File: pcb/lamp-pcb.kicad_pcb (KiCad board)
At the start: 2 copper layers, 0 parts

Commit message: board geometry mostly figured out
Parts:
- added C1: 0.1uF, passive-smd:0603(1608m), F.Cu at (99.7, 127.6)
- added C10: 0.1uF, passive-smd:0603(1608m), F.Cu at (165.7, 95.2)
- added C11: 0.1uF, passive-smd:0603(1608m), F.Cu at (163.2, 98.4)
- added C2: 24pF, passive-smd:0603(1608m), F.Cu at (101.6, 130.2)
- added C3: 24pF, passive-smd:0603(1608m), F.Cu at (106.7, 130.2)
- added C4: 0.1uF, passive-smd:0603(1608m), F.Cu at (98.4, 126.4)
- added C5: 0.1uF, passive-smd:0603(1608m), F.Cu at (111.8, 119.4)
- added C6: 0.1uF, passive-smd:0603(1608m), F.Cu at (110.5, 118.1)
- added C7: 10uF, passive-smd:1206(3216m), F.Cu at (100.3, 173.4)
- added C8: 22uF, passive-smd:1206(3216m), F.Cu at (100.3, 163.2)
- added C9: 0.1uF, passive-smd:0603(1608m), F.Cu at (99.7, 116.2)
- added IC1: ATMEGA328P, qfp:TQFP32_P0.8mm, F.Cu at (115.6, 156.8)
- added IC2: LM1117, sot:SOT223, F.Cu at (100.3, 168.3)
- added IC3: TLC5973, soic:SOIC8, F.Cu at (182.9, 81.9)
- added J1: 5V_OUT, sip:SIP2, F.Cu at (138.4, 174.0)
- added J2: LED_CARD_BOTTOM, sip:SIP5, F.Cu at (158.1, 88.9)
- added LED1: CREE-CLV6A-FKB, led:PLCC6-SM-RGB-LED, F.Cu at (176.5, 102.9)
- added LED2: CREE-CLV6A-FKB, led:PLCC6-SM-RGB-LED, F.Cu at (177.8, 93.3)
- added LED3: HEART, led:0603(1608m)-SM-LED, F.Cu at (111.8, 127.6)
- added LED4: PWR, led:0603(1608m)-SM-LED, F.Cu at (143.5, 137.2)
- added P1: 7-12V_IN, sip:SIP2, F.Cu at (92.7, 174.0)
- added P2: AVR_ISP, connect-thru:2x3-ARRAY_P100mil, F.Cu at (129.5, 167.6)
- added P3: SERIAL, sip:SIP6, F.Cu at (115.6, 140.3)
- added P4: LEDSTACK, sip:SIP5, F.Cu at (115.6, 173.4)
- added P5: LEDSTACK, sip:SIP5, F.Cu at (104.1, 151.8)
- added P6: LEDSTACK, sip:SIP5, F.Cu at (127.0, 152.4)
- added P7: LED_CARD_TOP, sip:SIP5, F.Cu at (167.6, 81.9)
- added R1: 10kΩ, passive-smd:0603(1608m), F.Cu at (101.6, 114.3)
- added R2: 10kΩ, passive-smd:0603(1608m), F.Cu at (106.7, 114.3)
- added R3: 10kΩ, passive-smd:0603(1608m), F.Cu at (108.6, 116.2)
- added R4: 2kΩ, passive-smd:0603(1608m), F.Cu at (191.1, 86.4)
- added R5: 1kΩ, passive-smd:0603(1608m), F.Cu at (195.6, 85.1)
- added R6: 1kΩ, passive-smd:0603(1608m), F.Cu at (111.8, 125.7)
- added R7: 1kΩ, passive-smd:0603(1608m), F.Cu at (143.5, 141.0)
- added S1: TOP, switch:CK-JS102011SAQN_sm-spdt-switch, F.Cu at (196.2, 97.8)
- added Y1: 14.7456MHz, crystal:HC49_sm, F.Cu at (115.6, 167.6)

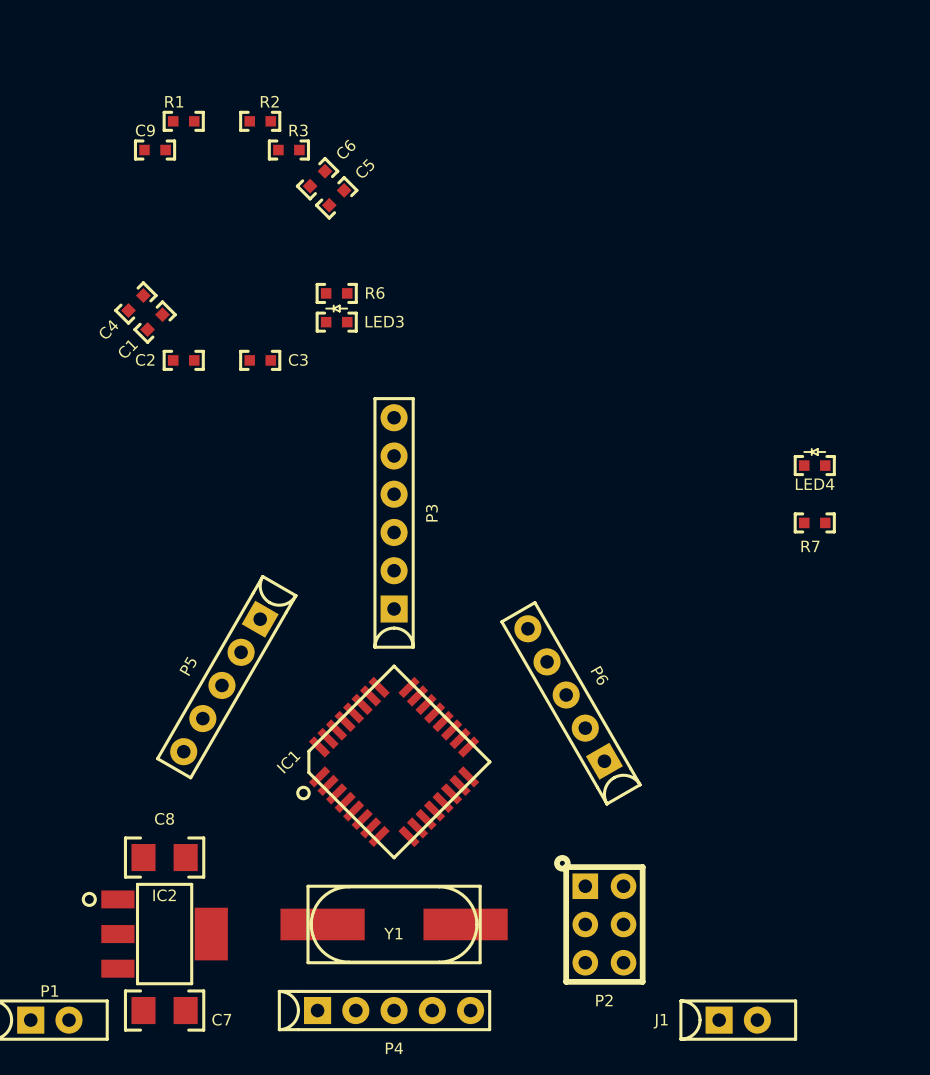
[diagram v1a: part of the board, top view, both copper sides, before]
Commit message: component positions good. need some mounting holes
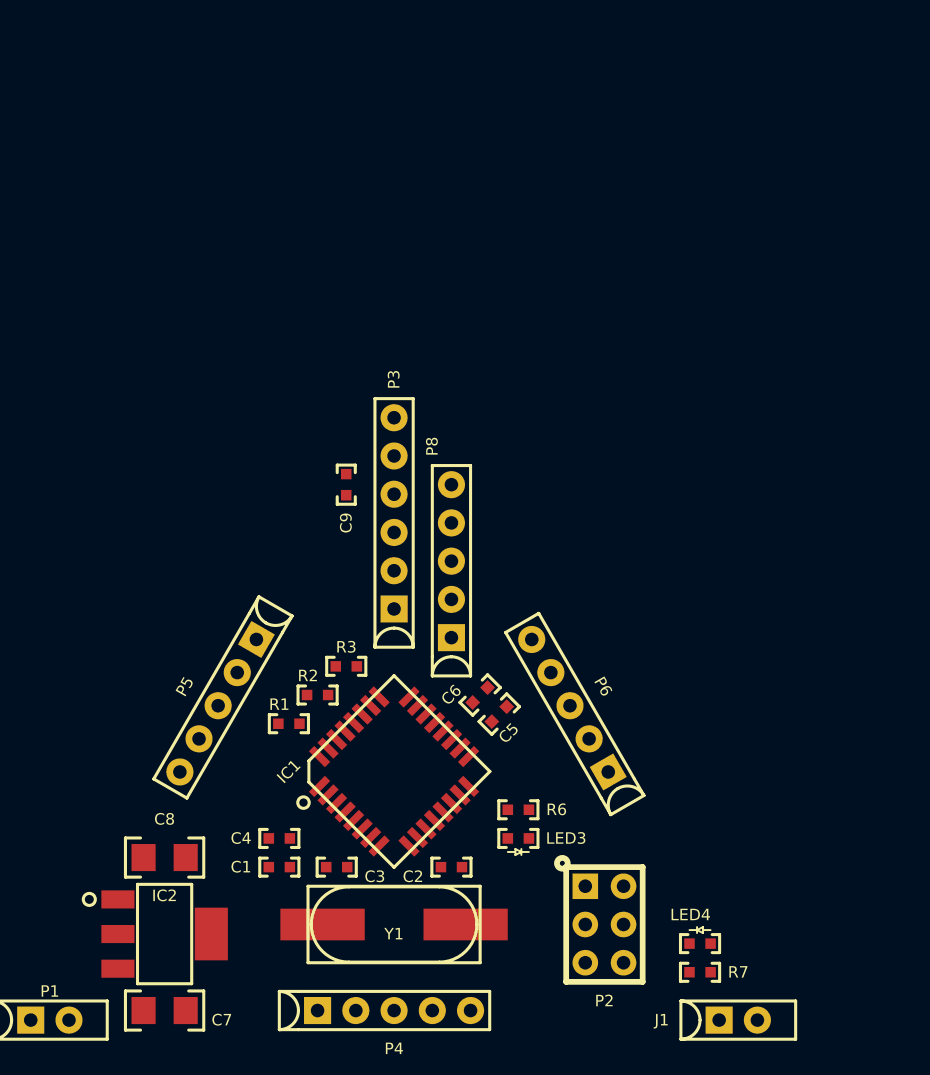
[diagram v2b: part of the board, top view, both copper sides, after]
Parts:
- added P8: SER_SHORT, sip:SIP5, F.Cu at (119.4, 143.5)
- moved R1 40.6 mm to (108.6, 154.3)
- moved R2 38.3 mm to (110.5, 152.4), turned to 180 degrees
- moved C2 38.1 mm to (119.4, 163.8), turned to 180 degrees
- moved C1 37.1 mm to (108.0, 163.8), turned to 180 degrees
- moved C4 36.8 mm to (108.0, 161.9), turned to 180 degrees
- moved LED3 36.4 mm to (123.8, 161.9), turned to 180 degrees
- moved R6 36.4 mm to (123.8, 160.0)
- moved C6 35.9 mm to (121.3, 152.4)
- moved C5 35.9 mm to (122.6, 153.7)
- moved R3 34.5 mm to (112.4, 150.5), turned to 180 degrees
- moved C3 34.0 mm to (111.8, 163.8), turned to 0 degrees
- moved LED4 32.7 mm to (135.9, 168.9)
- moved R7 30.8 mm to (135.9, 170.8)
- moved C9 25.6 mm to (112.4, 138.4), turned to 90 degrees
- moved P5 1.37 mm to (103.9, 153.1)
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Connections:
- IC1 pad 23: /STACKSENSE0 -> Net-(IC1-Pad23)
- IC1 pad 24: /STACKSENSE1 -> Net-(IC1-Pad24)
- IC1 pad 25: /STACKSENSE2 -> /STACKSENSE0
- IC1 pad 26: Net-(IC1-Pad26) -> /STACKSENSE1
- IC1 pad 27: Net-(IC1-Pad27) -> /STACKSENSE2

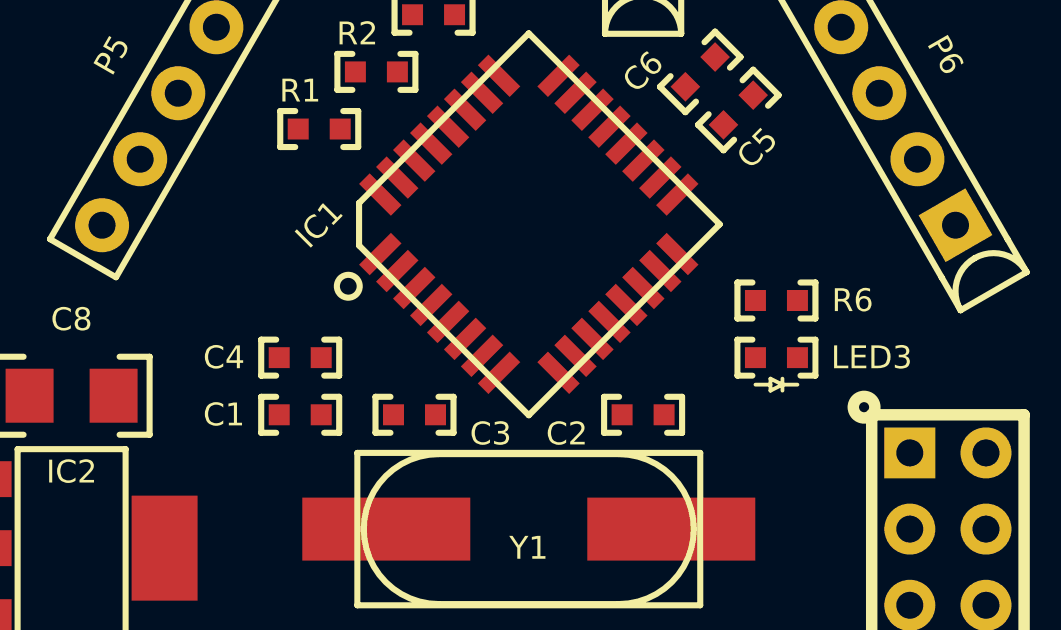
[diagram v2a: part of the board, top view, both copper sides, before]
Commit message: mounting holes
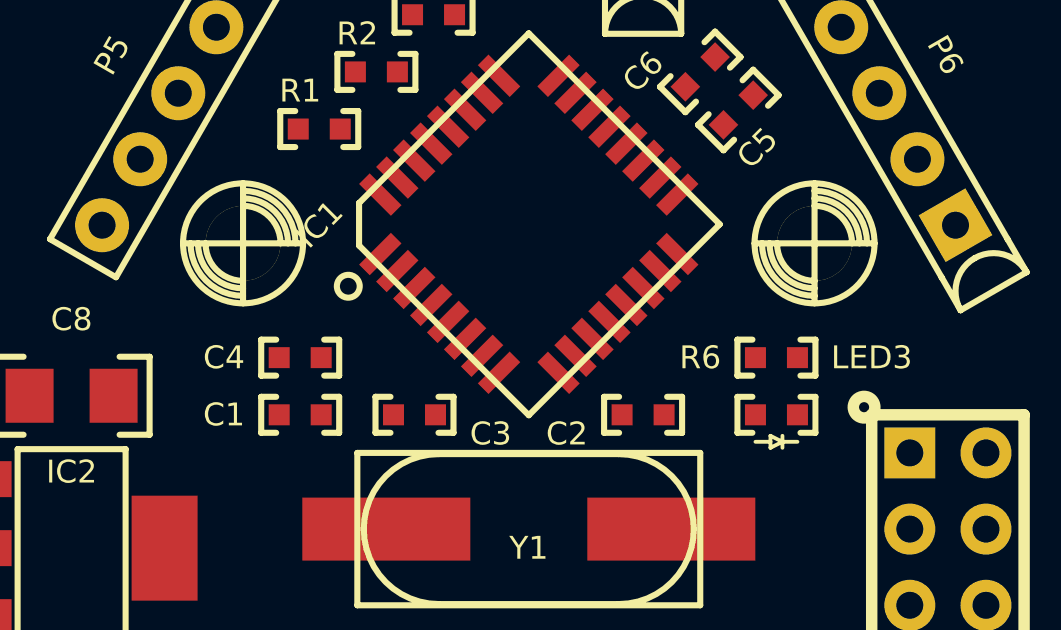
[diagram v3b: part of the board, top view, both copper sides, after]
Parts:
- added M2: Val**, asm:M2, F.Cu at (106.0, 158.1)
- added M2: Val**, asm:M2, F.Cu at (125.1, 158.1)
- moved LED3 1.91 mm to (123.8, 163.8)
- moved R6 1.91 mm to (123.8, 161.9)
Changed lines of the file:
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@@
 (kicad_pcb (version 3) (host pcbnew "(2014-02-03 BZR 4657)-product")
   (general
-    (links 100)
+    (links 0)
     (no_connects 100)
     (area 0 0 0 0)
@@
     (tracks 0)
     (zones 0)
-    (modules 37)
+    (modules 39)
     (nets 48)
   )
@@
   )
   (module "led:0603(1608m)-SM-LED" (layer F.Cu)
-    (at 123.825 161.925 180)
-    (solder_paste_margin -0.0254)
-    (attr smd)
-    (fp_text reference LED3 (at -3.175 0 180) (layer F.SilkS)
+    (at 123.825 163.83 180)
+    (solder_paste_margin -0.0254)
+    (attr smd)
+    (fp_text reference LED3 (at -3.175 1.905 180) (layer F.SilkS)
       (effects (font (size 0.762 0.762) (thickness 0.1524)))
     )
@@
   )
   (module "passive-smd:0603(1608m)" (layer F.Cu)
-    (at 123.825 160.02 180)
-    (solder_paste_margin -0.0254)
-    (attr smd)
-    (fp_text reference R6 (at -2.54 0 180) (layer F.SilkS)
+    (at 123.825 161.925 180)
+    (solder_paste_margin -0.0254)
+    (attr smd)
+    (fp_text reference R6 (at 2.54 0 180) (layer F.SilkS)
       (effects (font (size 0.762 0.762) (thickness 0.1524)))
     )
@@
       (net 20 /USART_TX))
   )
+  (module asm:M2 (layer F.Cu)
+    (at 106.045 158.115)
+    (fp_text reference M2 (at 0 0) (layer F.SilkS) hide
+      (effects (font (size 0.762 0.762) (thickness 0.1524)))
+    )
+    (fp_text value Val** (at 0 0) (layer F.SilkS) hide
+      (effects (font (size 0.762 0.762) (thickness 0.1524)))
+    )
+    (fp_arc (start 0 0) (end 0 1.25) (angle 90) (layer F.SilkS) (width 0.2032))
+    (fp_arc (start 0 0) (end 0 -1.25) (angle 90) (layer F.SilkS) (width 0.2032))
+    (fp_arc (start 0 0) (end 0 1.5) (angle 90) (layer F.SilkS) (width 0.2032))
+    (fp_arc (start 0 0) (end 0 1.75) (angle 90) (layer F.SilkS) (width 0.2032))
+    (fp_arc (start 0 0) (end 0 -1.5) (angle 90) (layer F.SilkS) (width 0.2032))
+    (fp_arc (start 0 0) (end 0 -1.75) (angle 90) (layer F.SilkS) (width 0.2032))
+    (fp_line (start 0 0) (end 0 2) (layer F.SilkS) (width 0.2032))
+    (fp_line (start 0 0) (end -2 0) (layer F.SilkS) (width 0.2032))
+    (fp_line (start 0 -2) (end 0 0) (layer F.SilkS) (width 0.2032))
+    (fp_line (start 0 0) (end 2 0) (layer F.SilkS) (width 0.2032))
+    (fp_circle (center 0 0) (end 2 0) (layer F.SilkS) (width 0.2032))
+    (pad "" thru_hole circle (at 0 0) (size 2.5 2.5) (drill 2.5) (layers *.Cu *.Mask F.SilkS))
+  )
+  (module asm:M2 (layer F.Cu)
+    (at 125.095 158.115)
+    (fp_text reference M2 (at 0 0) (layer F.SilkS) hide
+      (effects (font (size 0.762 0.762) (thickness 0.1524)))
+    )
+    (fp_text value Val** (at 0 0) (layer F.SilkS) hide
+      (effects (font (size 0.762 0.762) (thickness 0.1524)))
+    )
+    (fp_arc (start 0 0) (end 0 1.25) (angle 90) (layer F.SilkS) (width 0.2032))
+    (fp_arc (start 0 0) (end 0 -1.25) (angle 90) (layer F.SilkS) (width 0.2032))
+    (fp_arc (start 0 0) (end 0 1.5) (angle 90) (layer F.SilkS) (width 0.2032))
+    (fp_arc (start 0 0) (end 0 1.75) (angle 90) (layer F.SilkS) (width 0.2032))
+    (fp_arc (start 0 0) (end 0 -1.5) (angle 90) (layer F.SilkS) (width 0.2032))
+    (fp_arc (start 0 0) (end 0 -1.75) (angle 90) (layer F.SilkS) (width 0.2032))
+    (fp_line (start 0 0) (end 0 2) (layer F.SilkS) (width 0.2032))
+    (fp_line (start 0 0) (end -2 0) (layer F.SilkS) (width 0.2032))
+    (fp_line (start 0 -2) (end 0 0) (layer F.SilkS) (width 0.2032))
+    (fp_line (start 0 0) (end 2 0) (layer F.SilkS) (width 0.2032))
+    (fp_circle (center 0 0) (end 2 0) (layer F.SilkS) (width 0.2032))
+    (pad "" thru_hole circle (at 0 0) (size 2.5 2.5) (drill 2.5) (layers *.Cu *.Mask F.SilkS))
+  )
   (dimension 46.355 (width 0.254) (layer Eco2.User)

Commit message: laying traces
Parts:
- moved C4 75.2 mm to (92.7, 88.3)
- moved C1 74.6 mm to (92.7, 90.8)
- moved C2 74.6 mm to (104.1, 90.8)
- moved C3 74.6 mm to (96.5, 90.8)
- moved C6 74.6 mm to (106.0, 79.4)
- moved C9 74.6 mm to (97.2, 65.4)
- moved IC2 74.6 mm to (85.1, 95.2)
- moved J1 74.6 mm to (123.2, 101.0)
- moved LED3 74.6 mm to (108.6, 90.8)
- moved M2 74.6 mm to (90.8, 85.1)
- moved M2 74.6 mm to (109.9, 85.1)
- moved P1 74.6 mm to (77.5, 101.0)
- moved P3 74.6 mm to (100.3, 67.3)
- moved R1 74.6 mm to (93.3, 81.3)
- moved R2 74.6 mm to (95.2, 79.4)
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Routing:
- net VCC: track 0.00 -> 45.4 mm
- net /USART_TX: track 0.00 -> 32.8 mm, vias 0 -> 2
- net GND: track 0.00 -> 26.5 mm
- net /USART_RX: track 0.00 -> 25.7 mm, vias 0 -> 2
- net /AVR_RST: track 0.00 -> 20.0 mm, vias 0 -> 2
- net /AVR_SCK: track 0.00 -> 19.3 mm, vias 0 -> 1
- net /AVR_MOSI: track 0.00 -> 16.7 mm
- net /STACKSENSE1: track 0.00 -> 16.1 mm, vias 0 -> 1
- net /LEDSTACK1: track 0.00 -> 12.3 mm
- net /AVR_MISO: track 0.00 -> 11.6 mm
- net Net-(C9-Pad2): track 0.00 -> 11.5 mm
- net Net-(C2-Pad2): track 0.00 -> 10.9 mm
- net Net-(C3-Pad2): track 0.00 -> 7.10 mm
- net Net-(IC1-Pad13): track 0.00 -> 5.03 mm
- net /STACKSENSE2: track 0.00 -> 4.95 mm
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- added copper zone on F.Cu, net /VIN
- added copper zone on F.Cu, net VCC
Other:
- board outline added: 53.3 x 46.4 mm
- net class Default: via_dia 0.889 -> 0.762; via_drill 0.635 -> 0.381
- rule trace_min: 0.254 -> 0.1524
- rule via_min_drill: 0.508 -> 0.3556
- rule via_min_size: 0.889 -> 0.7112

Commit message: layout going well but computer dying
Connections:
- R4 pad 2: GND -> /LED_GND
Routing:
- net /STACKSENSE0: track 2.65 -> 41.5 mm, vias 0 -> 1
- net /LEDSTACK0: track 0.00 -> 32.6 mm, vias 0 -> 1
- net /LEDSTACK2: track 0.00 -> 19.6 mm, vias 0 -> 1
- net VCC: track 45.4 -> 64.8 mm
- net /STACKSENSE2: track 4.95 -> 21.6 mm, vias 0 -> 1
- added copper zone on B.Cu, net GND
- added copper zone on F.Cu, net GND
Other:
- outline, holes or cut-outs redrawn

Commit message: layout done. getting quotes then gonna clean up
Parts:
- added M2: Val**, asm:M2, F.Cu at (176.5, 144.8)
- added M2: Val**, asm:M2, F.Cu at (154.9, 127.0)
- moved R4 57.0 mm to (175.5, 141.2), turned to 270 degrees
- moved J2 57.0 mm to (165.7, 145.4)
- moved S1 56.2 mm to (154.9, 135.9), turned to 270 degrees
- moved IC3 54.5 mm to (175.3, 135.9), turned to 270 degrees
- moved LED2 47.9 mm to (165.7, 139.7), turned to 180 degrees
- moved C11 47.5 mm to (156.2, 145.4), turned to 180 degrees
- moved C10 47.4 mm to (177.2, 141.2), turned to 90 degrees
- moved R5 46.0 mm to (175.3, 126.4), turned to 180 degrees
- moved P7 44.5 mm to (165.7, 126.4)
- moved LED1 31.1 mm to (165.7, 132.1), turned to 180 degrees
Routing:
- net /VIN: track 0.00 -> 74.9 mm, vias 0 -> 1
- net VCC: track 64.8 -> 120.2 mm
- net /VLOG: track 0.00 -> 36.0 mm, vias 0 -> 2
- net /SENSE_TOP: track 0.00 -> 35.9 mm, vias 0 -> 1
- net /VLED: track 0.00 -> 30.6 mm
- net GND: track 26.5 -> 52.9 mm, vias 0 -> 3
- net /AVR_RST: track 20.0 -> 43.7 mm, vias 2 -> 3
- net /SENSE_BOT: track 0.00 -> 23.0 mm, vias 0 -> 1
- net /LED_SER_OUT: track 0.00 -> 22.0 mm, vias 0 -> 2
- net Net-(LED1-Pad5): track 0.00 -> 12.4 mm
- net Net-(LED1-Pad4): track 0.00 -> 12.0 mm
- net Net-(LED1-Pad6): track 0.00 -> 11.1 mm
- net /LED_SER_IN: track 0.00 -> 10.9 mm
- net /VLOG_TOP: track 0.00 -> 10.8 mm, vias 0 -> 1
- net /RED: track 0.00 -> 10.6 mm
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- added copper zone on B.Cu, net /LED_GND
- added copper zone on F.Cu, net /LED_GND
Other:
- board size 53.3 x 46.4 mm -> 105.4 x 91.4 mm
- net class LED added: clearance 0.3048, trace_width 0.3048, via_dia 0.762, via_drill 0.381
- net class VIN added: clearance 0.508, trace_width 0.508, via_dia 0.889, via_drill 0.508
